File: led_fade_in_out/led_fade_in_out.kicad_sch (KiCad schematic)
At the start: 6 parts, among them Q1 PN2222A, SW1 SW_SPST

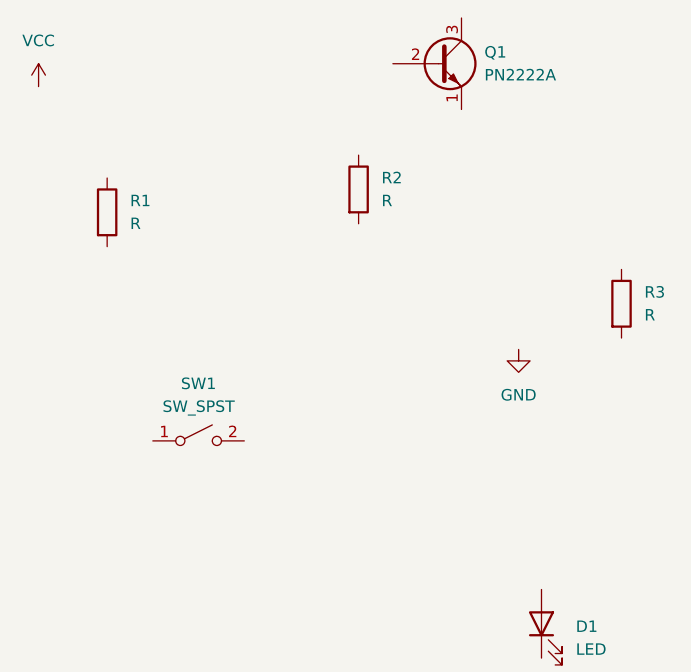
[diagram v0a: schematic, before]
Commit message: place fader components
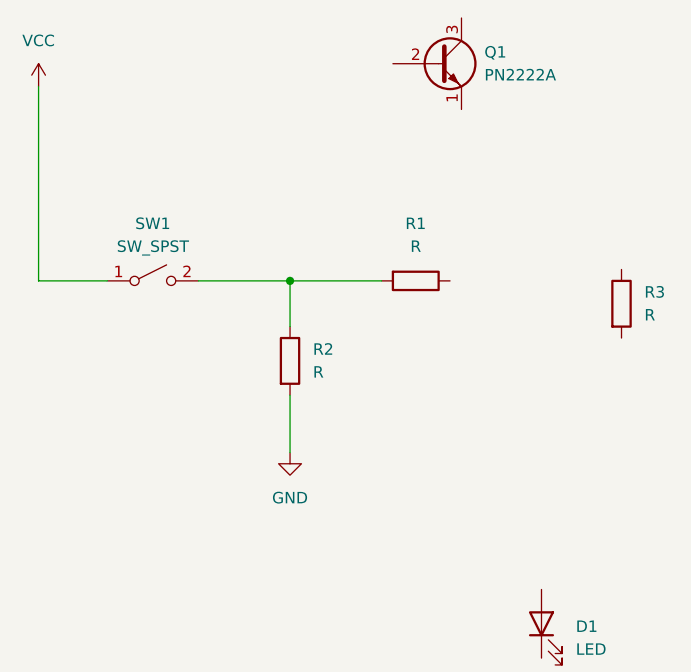
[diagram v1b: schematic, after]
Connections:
- net GND: now also R2.2
- net VCC: now also SW1.1 (A)
- net at SW1.2 (B): now also R1.2, R2.1
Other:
- moved on the sheet: R1, R2, SW1
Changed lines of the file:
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@@
 (kicad_sch (version 20230121) (generator eeschema)
   (paper "A4")
+  (junction (at 144.78 90.17) (diameter 0) (color 0 0 0 0)
+  )
+  (wire (pts (xy 154.94 90.17) (xy 144.78 90.17))
+    (stroke (width 0) (type default))
+  )
+  (wire (pts (xy 116.84 90.17) (xy 116.84 68.58))
+    (stroke (width 0) (type default))
+  )
+  (wire (pts (xy 144.78 90.17) (xy 144.78 95.25))
+    (stroke (width 0) (type default))
+  )
+  (wire (pts (xy 144.78 102.87) (xy 144.78 109.22))
+    (stroke (width 0) (type default))
+  )
+  (wire (pts (xy 134.62 90.17) (xy 144.78 90.17))
+    (stroke (width 0) (type default))
+  )
+  (wire (pts (xy 124.46 90.17) (xy 116.84 90.17))
+    (stroke (width 0) (type default))
+  )
   (symbol (lib_id "Device:R") (at 181.61 92.71 0) (unit 1)
     (in_bom yes) (on_board yes) (dnp no) (fields_autoplaced)
@@
     )
   )
-  (symbol (lib_id "power:GND") (at 170.18 97.79 0) (unit 1)
-    (in_bom yes) (on_board yes) (dnp no) (fields_autoplaced)
-    (property "Reference" "#PWR02" (at 170.18 104.14 0)
-      (effects (font (size 1.27 1.27)) hide)
-    )
-    (property "Value" "GND" (at 170.18 102.87 0)
-      (effects (font (size 1.27 1.27)))
-    )
-    (property "Footprint" "" (at 170.18 97.79 0)
-      (effects (font (size 1.27 1.27)) hide)
-    )
-    (property "Datasheet" "" (at 170.18 97.79 0)
+  (symbol (lib_id "power:GND") (at 144.78 109.22 0) (unit 1)
+    (in_bom yes) (on_board yes) (dnp no) (fields_autoplaced)
+    (property "Reference" "#PWR02" (at 144.78 115.57 0)
+      (effects (font (size 1.27 1.27)) hide)
+    )
+    (property "Value" "GND" (at 144.78 114.3 0)
+      (effects (font (size 1.27 1.27)))
+    )
+    (property "Footprint" "" (at 144.78 109.22 0)
+      (effects (font (size 1.27 1.27)) hide)
+    )
+    (property "Datasheet" "" (at 144.78 109.22 0)
       (effects (font (size 1.27 1.27)) hide)
     )
@@
     )
   )
-  (symbol (lib_id "Switch:SW_SPST") (at 134.62 107.95 0) (unit 1)
-    (in_bom yes) (on_board yes) (dnp no) (fields_autoplaced)
-    (property "Reference" "SW1" (at 134.62 101.6 0)
-      (effects (font (size 1.27 1.27)))
-    )
-    (property "Value" "SW_SPST" (at 134.62 104.14 0)
-      (effects (font (size 1.27 1.27)))
-    )
-    (property "Footprint" "" (at 134.62 107.95 0)
-      (effects (font (size 1.27 1.27)) hide)
-    )
-    (property "Datasheet" "~" (at 134.62 107.95 0)
+  (symbol (lib_id "Switch:SW_SPST") (at 129.54 90.17 0) (unit 1)
+    (in_bom yes) (on_board yes) (dnp no) (fields_autoplaced)
+    (property "Reference" "SW1" (at 129.54 83.82 0)
+      (effects (font (size 1.27 1.27)))
+    )
+    (property "Value" "SW_SPST" (at 129.54 86.36 0)
+      (effects (font (size 1.27 1.27)))
+    )
+    (property "Footprint" "" (at 129.54 90.17 0)
+      (effects (font (size 1.27 1.27)) hide)
+    )
+    (property "Datasheet" "~" (at 129.54 90.17 0)
       (effects (font (size 1.27 1.27)) hide)
     )
@@
     )
   )
-  (symbol (lib_id "Device:R") (at 152.4 80.01 0) (unit 1)
-    (in_bom yes) (on_board yes) (dnp no) (fields_autoplaced)
-    (property "Reference" "R2" (at 154.94 78.74 0)
-      (effects (font (size 1.27 1.27)) (justify left))
-    )
-    (property "Value" "R" (at 154.94 81.28 0)
-      (effects (font (size 1.27 1.27)) (justify left))
-    )
-    (property "Footprint" "" (at 150.622 80.01 90)
-      (effects (font (size 1.27 1.27)) hide)
-    )
-    (property "Datasheet" "~" (at 152.4 80.01 0)
+  (symbol (lib_id "Device:R") (at 144.78 99.06 0) (unit 1)
+    (in_bom yes) (on_board yes) (dnp no) (fields_autoplaced)
+    (property "Reference" "R2" (at 147.32 97.79 0)
+      (effects (font (size 1.27 1.27)) (justify left))
+    )
+    (property "Value" "R" (at 147.32 100.33 0)
+      (effects (font (size 1.27 1.27)) (justify left))
+    )
+    (property "Footprint" "" (at 143.002 99.06 90)
+      (effects (font (size 1.27 1.27)) hide)
+    )
+    (property "Datasheet" "~" (at 144.78 99.06 0)
       (effects (font (size 1.27 1.27)) hide)
     )
@@
     )
   )
-  (symbol (lib_id "Device:R") (at 124.46 82.55 0) (unit 1)
-    (in_bom yes) (on_board yes) (dnp no) (fields_autoplaced)
-    (property "Reference" "R1" (at 127 81.28 0)
-      (effects (font (size 1.27 1.27)) (justify left))
-    )
-    (property "Value" "R" (at 127 83.82 0)
-      (effects (font (size 1.27 1.27)) (justify left))
-    )
-    (property "Footprint" "" (at 122.682 82.55 90)
-      (effects (font (size 1.27 1.27)) hide)
-    )
-    (property "Datasheet" "~" (at 124.46 82.55 0)
-      (effects (font (size 1.27 1.27)) hide)
-    )
+  (symbol (lib_id "Device:R") (at 158.75 90.17 270) (unit 1)
+    (in_bom yes) (on_board yes) (dnp no) (fields_autoplaced)
+    (property "Reference" "R1" (at 158.75 83.82 90)
+      (effects (font (size 1.27 1.27)))
+    )
+    (property "Value" "R" (at 158.75 86.36 90)
+      (effects (font (size 1.27 1.27)))
+    )
+    (property "Footprint" "" (at 158.75 88.392 90)
+      (effects (font (size 1.27 1.27)) hide)
+    )
+    (property "Datasheet" "~" (at 158.75 90.17 0)
+      (effects (font (size 1.27 1.27)) hide)
+    )

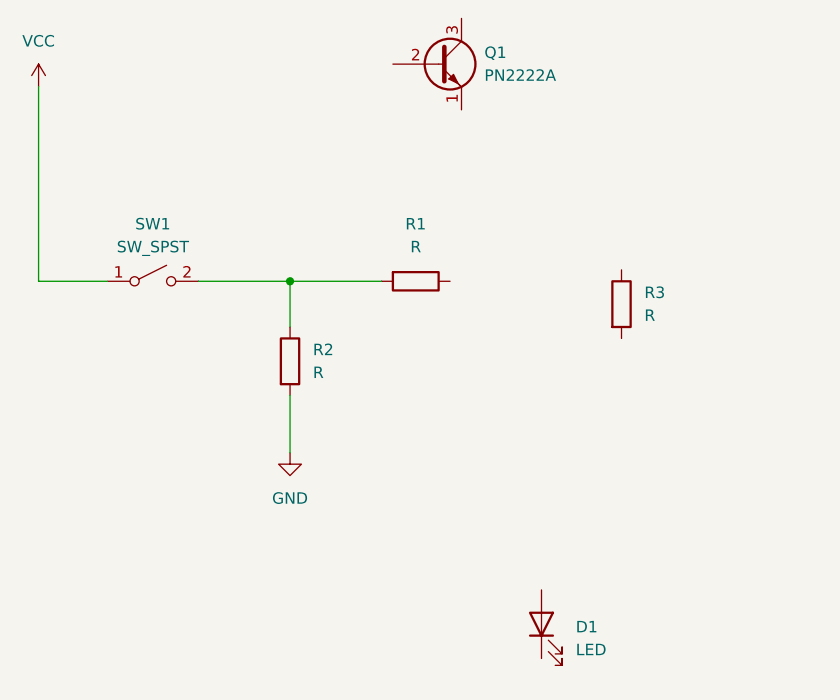
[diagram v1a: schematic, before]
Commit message: add component values
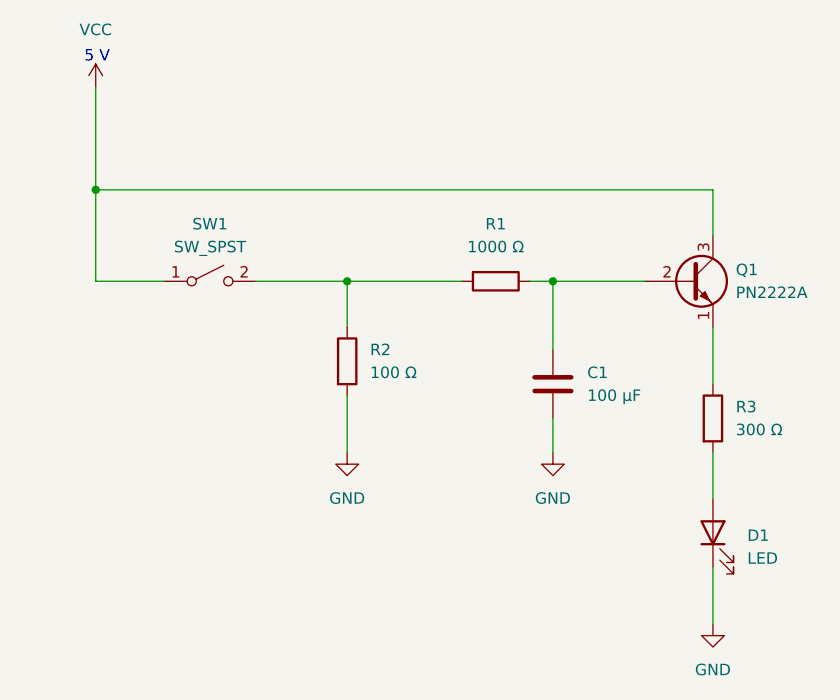
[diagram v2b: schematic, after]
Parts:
- added C1: 100 µF, symbol Device:C
- R1: value R -> 1000 Ω
- R2: value R -> 100 Ω
- R3: value R -> 300 Ω
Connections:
- net GND: now also D1.1 (K), C1.2
- net VCC: now also Q1.3 (C)
- net at R3.1: now also Q1.1 (E)
- net at R3.2: now also D1.2 (A)
- net at Q1.2 (B): now also R1.1, C1.1
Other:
- note added: "5 V"
- moved on the sheet: D1, Q1, R1, R2, R3, SW1

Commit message: fix spacing
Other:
- note added: "Transistor (https://electronics.stackexchange.com/users/73158/transistor), Simple LED fade circuit, URL (version: 2018-11-07): https://electronics.stackexchange.com/q/405503"
- moved on the sheet: D1, R2, R3
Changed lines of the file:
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@@
     (stroke (width 0) (type default))
   )
-  (wire (pts (xy 151.13 90.17) (xy 151.13 95.25))
+  (wire (pts (xy 151.13 90.17) (xy 151.13 97.79))
     (stroke (width 0) (type default))
   )
@@
     (stroke (width 0) (type default))
   )
-  (wire (pts (xy 151.13 102.87) (xy 151.13 109.22))
-    (stroke (width 0) (type default))
-  )
-  (wire (pts (xy 191.77 95.25) (xy 191.77 101.6))
+  (wire (pts (xy 191.77 95.25) (xy 191.77 97.79))
     (stroke (width 0) (type default))
   )
@@
     (stroke (width 0) (type default))
   )
-  (wire (pts (xy 191.77 109.22) (xy 191.77 114.3))
+  (wire (pts (xy 191.77 105.41) (xy 191.77 109.22))
     (stroke (width 0) (type default))
   )
@@
     (stroke (width 0) (type default))
   )
-  (wire (pts (xy 191.77 121.92) (xy 191.77 128.27))
+  (wire (pts (xy 191.77 116.84) (xy 191.77 125.73))
     (stroke (width 0) (type default))
   )
@@
     (stroke (width 0) (type default))
   )
-  (wire (pts (xy 173.99 109.22) (xy 173.99 105.41))
+  (wire (pts (xy 151.13 105.41) (xy 151.13 110.49))
+    (stroke (width 0) (type default))
+  )
+  (wire (pts (xy 173.99 110.49) (xy 173.99 105.41))
     (stroke (width 0) (type default))
   )
   (wire (pts (xy 123.19 68.58) (xy 123.19 80.01))
     (stroke (width 0) (type default))
+  )
+  (text "Transistor (https://electronics.stackexchange.com/users/73158/transistor), Simple LED fade circuit, \nURL (version: 2018-11-07): https://electronics.stackexchange.com/q/405503"
+    (at 179.07 171.45 0)
+    (effects (font (size 1.27 1.27)) (justify left bottom))
   )
   (text "5 V" (at 121.92 66.04 0)
     (effects (font (size 1.27 1.27)) (justify left bottom))
   )
-  (symbol (lib_id "Device:R") (at 191.77 105.41 0) (unit 1)
-    (in_bom yes) (on_board yes) (dnp no)
-    (property "Reference" "R3" (at 194.31 104.14 0)
-      (effects (font (size 1.27 1.27)) (justify left))
-    )
-    (property "Value" "300 Ω" (at 194.31 106.68 0)
-      (effects (font (size 1.27 1.27)) (justify left))
-    )
-    (property "Footprint" "" (at 189.992 105.41 90)
-      (effects (font (size 1.27 1.27)) hide)
-    )
-    (property "Datasheet" "~" (at 191.77 105.41 0)
+  (symbol (lib_id "Device:R") (at 191.77 101.6 0) (unit 1)
+    (in_bom yes) (on_board yes) (dnp no)
+    (property "Reference" "R3" (at 194.31 100.33 0)
+      (effects (font (size 1.27 1.27)) (justify left))
+    )
+    (property "Value" "300 Ω" (at 194.31 102.87 0)
+      (effects (font (size 1.27 1.27)) (justify left))
+    )
+    (property "Footprint" "" (at 189.992 101.6 90)
+      (effects (font (size 1.27 1.27)) hide)
+    )
+    (property "Datasheet" "~" (at 191.77 101.6 0)
       (effects (font (size 1.27 1.27)) hide)
     )
@@
     )
   )
-  (symbol (lib_id "power:GND") (at 151.13 109.22 0) (unit 1)
-    (in_bom yes) (on_board yes) (dnp no) (fields_autoplaced)
-    (property "Reference" "#PWR02" (at 151.13 115.57 0)
-      (effects (font (size 1.27 1.27)) hide)
-    )
-    (property "Value" "GND" (at 151.13 114.3 0)
-      (effects (font (size 1.27 1.27)))
-    )
-    (property "Footprint" "" (at 151.13 109.22 0)
-      (effects (font (size 1.27 1.27)) hide)
-    )
-    (property "Datasheet" "" (at 151.13 109.22 0)
+  (symbol (lib_id "power:GND") (at 151.13 110.49 0) (unit 1)
+    (in_bom yes) (on_board yes) (dnp no) (fields_autoplaced)
+    (property "Reference" "#PWR02" (at 151.13 116.84 0)
+      (effects (font (size 1.27 1.27)) hide)
+    )
+    (property "Value" "GND" (at 151.13 115.57 0)
+      (effects (font (size 1.27 1.27)))
+    )
+    (property "Footprint" "" (at 151.13 110.49 0)
+      (effects (font (size 1.27 1.27)) hide)
+    )
+    (property "Datasheet" "" (at 151.13 110.49 0)
       (effects (font (size 1.27 1.27)) hide)
     )
@@
     )
   )
-  (symbol (lib_id "Device:LED") (at 191.77 118.11 90) (unit 1)
-    (in_bom yes) (on_board yes) (dnp no)
-    (property "Reference" "D1" (at 195.58 118.4275 90)
+  (symbol (lib_id "Device:LED") (at 191.77 113.03 90) (unit 1)
+    (in_bom yes) (on_board yes) (dnp no)
+    (property "Reference" "D1" (at 195.58 113.3475 90)
       (effects (font (size 1.27 1.27)) (justify right))
     )
-    (property "Value" "LED" (at 195.58 120.9675 90)
+    (property "Value" "LED" (at 195.58 115.8875 90)
       (effects (font (size 1.27 1.27)) (justify right))
     )
-    (property "Footprint" "" (at 191.77 118.11 0)
-      (effects (font (size 1.27 1.27)) hide)
-    )
-    (property "Datasheet" "~" (at 191.77 118.11 0)
+    (property "Footprint" "" (at 191.77 113.03 0)
+      (effects (font (size 1.27 1.27)) hide)
+    )
+    (property "Datasheet" "~" (at 191.77 113.03 0)
       (effects (font (size 1.27 1.27)) hide)
     )
@@
     )
   )
-  (symbol (lib_id "power:GND") (at 173.99 109.22 0) (unit 1)
-    (in_bom yes) (on_board yes) (dnp no) (fields_autoplaced)
-    (property "Reference" "#PWR04" (at 173.99 115.57 0)
-      (effects (font (size 1.27 1.27)) hide)
-    )
-    (property "Value" "GND" (at 173.99 114.3 0)
-      (effects (font (size 1.27 1.27)))
-    )
-    (property "Footprint" "" (at 173.99 109.22 0)
-      (effects (font (size 1.27 1.27)) hide)
-    )
-    (property "Datasheet" "" (at 173.99 109.22 0)
+  (symbol (lib_id "power:GND") (at 173.99 110.49 0) (unit 1)
+    (in_bom yes) (on_board yes) (dnp no) (fields_autoplaced)
+    (property "Reference" "#PWR04" (at 173.99 116.84 0)
+      (effects (font (size 1.27 1.27)) hide)
+    )
+    (property "Value" "GND" (at 173.99 115.57 0)
+      (effects (font (size 1.27 1.27)))
+    )
+    (property "Footprint" "" (at 173.99 110.49 0)
+      (effects (font (size 1.27 1.27)) hide)
+    )
+    (property "Datasheet" "" (at 173.99 110.49 0)
       (effects (font (size 1.27 1.27)) hide)
     )
@@
     )
   )
-  (symbol (lib_id "Device:R") (at 151.13 99.06 0) (unit 1)
-    (in_bom yes) (on_board yes) (dnp no) (fields_autoplaced)
-    (property "Reference" "R2" (at 153.67 97.79 0)
-      (effects (font (size 1.27 1.27)) (justify left))
-    )
-    (property "Value" "100 Ω" (at 153.67 100.33 0)
-      (effects (font (size 1.27 1.27)) (justify left))
-    )
-    (property "Footprint" "" (at 149.352 99.06 90)
-      (effects (font (size 1.27 1.27)) hide)
-    )
-    (property "Datasheet" "~" (at 151.13 99.06 0)
+  (symbol (lib_id "Device:R") (at 151.13 101.6 0) (unit 1)
+    (in_bom yes) (on_board yes) (dnp no) (fields_autoplaced)
+    (property "Reference" "R2" (at 153.67 100.33 0)
+      (effects (font (size 1.27 1.27)) (justify left))
+    )
+    (property "Value" "100 Ω" (at 153.67 102.87 0)
+      (effects (font (size 1.27 1.27)) (justify left))
+    )
+    (property "Footprint" "" (at 149.352 101.6 90)
+      (effects (font (size 1.27 1.27)) hide)
+    )
+    (property "Datasheet" "~" (at 151.13 101.6 0)
       (effects (font (size 1.27 1.27)) hide)
     )
@@
     )
   )
-  (symbol (lib_id "power:GND") (at 191.77 128.27 0) (unit 1)
-    (in_bom yes) (on_board yes) (dnp no) (fields_autoplaced)
-    (property "Reference" "#PWR03" (at 191.77 134.62 0)
-      (effects (font (size 1.27 1.27)) hide)
-    )
-    (property "Value" "GND" (at 191.77 133.35 0)
-      (effects (font (size 1.27 1.27)))
-    )
-    (property "Footprint" "" (at 191.77 128.27 0)
-      (effects (font (size 1.27 1.27)) hide)
-    )
-    (property "Datasheet" "" (at 191.77 128.27 0)
-      (effects (font (size 1.27 1.27)) hide)
-    )
+  (symbol (lib_id "power:GND") (at 191.77 125.73 0) (unit 1)
+    (in_bom yes) (on_board yes) (dnp no) (fields_autoplaced)
+    (property "Reference" "#PWR03" (at 191.77 132.08 0)
+      (effects (font (size 1.27 1.27)) hide)
+    )
+    (property "Value" "GND" (at 191.77 130.81 0)
+      (effects (font (size 1.27 1.27)))
+    )
+    (property "Footprint" "" (at 191.77 125.73 0)
+      (effects (font (size 1.27 1.27)) hide)
+    )
+    (property "Datasheet" "" (at 191.77 125.73 0)
+      (effects (font (size 1.27 1.27)) hide)
+    )
